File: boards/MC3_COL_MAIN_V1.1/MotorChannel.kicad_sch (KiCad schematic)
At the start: 8 parts, among them J7 MOTOR, U3 DRV8214RTER

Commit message: V1.1: encoder FFC VIN on filtered VSENS, motor pads off MotorChannel, yaw nets renamed
- Connectors: encoder FFC VIN now fed from VSENS (VM through FB61 + C63);
  ENC_leaf1-4 / RC_OUT labels re-placed; SIG pull-ups to +3V3 noted on sheet
- MotorChannel: J7-J9 MOTOR pad connectors (Conn_01x02) and their OUT1/OUT2
  hierarchical labels removed from the shared sheet
- MCU: ENC_leaf1-4 global labels re-placed; sheet notes carried over
- Root: H5 SLOT-PASSTHRU mounting hole removed
- PCB: yaw motor nets YAW_OUT* -> /yaw/OUT*; CANH/CANL pad assignment swapped;
  VSENS/VM net reassignments and follow-up routing (~106 segments, 12 vias,
  zone edits) to match the schematic

Co-Authored-By: Claude Fable 5 <noreply@anthropic.com>
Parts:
- removed J7: MOTOR, MC3_COL_MAIN:SolderPads_2x_2.2x1.4mm_P2.6mm, symbol Connector_Generic:Conn_01x02
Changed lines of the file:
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@@
-		)
-	)
-	(label "OUT1"
-		(at 144.78 95.25 180)
-		(effects
-			(font
-				(size 1.27 1.27)
-			)
-			(justify right bottom)
-		)
-	)
-	(label "OUT2"
-		(at 144.78 97.79 180)
-		(effects
-			(font
-				(size 1.27 1.27)
-			)
-			(justify right bottom)
 		)
 	)
@@
 				)
 			)
-		)
-	)
-	(hierarchical_label "OUT1"
-		(shape output)
-		(at 144.78 95.25 180)
-		(effects
-			(font
-				(size 1.27 1.27)
-			)
-			(justify right)
-		)
-	)
-	(hierarchical_label "OUT2"
-		(shape output)
-		(at 144.78 97.79 180)
-		(effects
-			(font
-				(size 1.27 1.27)
-			)
-			(justify right)
 		)
 	)
@@
 					(unit 1)
 				)
-			)
-		)
-	)
-	(symbol
-		(lib_id "Connector_Generic:Conn_01x02")
-		(at 149.86 95.25 0)
-		(unit 1)
-		(body_style 1)
-		(exclude_from_sim no)
-		(in_bom yes)
-		(on_board yes)
-		(in_pos_files yes)
-		(dnp no)
-		(property "Reference" "J7"
-			(at 149.86 92.71 0)
-			(show_name no)
-			(do_not_autoplace no)
-			(effects
-				(font
-					(size 1.27 1.27)
-				)
-			)
-		)
-		(property "Value" "MOTOR"
-			(at 149.86 100.33 0)
-			(show_name no)
-			(do_not_autoplace no)
-			(effects
-				(font
-					(size 1.27 1.27)
-				)
-			)
-		)
-		(property "Footprint" "MC3_COL_MAIN:SolderPads_2x_2.2x1.4mm_P2.6mm"
-			(at 149.86 95.25 0)
-			(hide yes)
-			(show_name no)
-			(do_not_autoplace no)
-			(effects
-				(font
-					(size 1.27 1.27)
-				)
-			)
-		)
-		(property "Datasheet" ""
-			(at 149.86 95.25 0)
-			(hide yes)
-			(show_name no)
-			(do_not_autoplace no)
-			(effects
-				(font
-					(size 1.27 1.27)
-				)
-			)
-		)
-		(property "Description" ""
-			(at 149.86 95.25 0)
-			(show_name no)
-			(do_not_autoplace no)
-			(effects
-				(font
-					(size 1.27 1.27)
-				)
-			)
-		)
-		(property "Note" "Bare solder pads 2.2x1.4 @2.6 mm, no part - vault Main-Board-01 Connectors, Motor Terminations"
-			(at 149.86 95.25 0)
-			(hide yes)
-			(show_name no)
-			(do_not_autoplace no)
-			(effects
-				(font
-					(size 1.27 1.27)
-				)
-			)
-		)
-		(pin "2"
-		)
-		(pin "1"
-		)
-		(instances
-			(project "MC3_COL_MAIN_V1.1"
-				(path "/7d5f4202-d55e-4c7b-a2df-dd599db38e48/5db6fbb9-0012-419b-b34a-9d86ac1f5217"
-					(reference "J8")
-					(unit 1)
-				)
-				(path "/7d5f4202-d55e-4c7b-a2df-dd599db38e48/8cfd3b4a-99dc-4b05-a7ad-f8199ec40931"
-					(reference "J11")
-					(unit 1)
-				)
-				(path "/7d5f4202-d55e-4c7b-a2df-dd599db38e48/9d20a086-3ce1-4783-a1c3-78685ff35655"
-					(reference "J10")
-					(unit 1)
-				)
-				(path "/7d5f4202-d55e-4c7b-a2df-dd599db38e48/a93ffbcb-09b2-46f4-87ff-b0a1b53638e4"
-					(reference "J7")
-					(unit 1)
-				)
-				(path "/7d5f4202-d55e-4c7b-a2df-dd599db38e48/f0c3363d-cc6b-4f74-be1d-ed0c2c093cdf"
-					(reference "J9")
-					(unit 1)
-				)
-			)
-			(project "MotorChannel"
-				(path "/d4aaa694-2c98-4a3a-bc8f-3a2af1030686"
-					(reference "J1")
-					(unit 1)
-				)

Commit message: V1.1: power routing pass — 24V chain + buck routed, stale-net/short fixes, VQFN corner pads fused, yaw OUT hier labels restored
- Board: VIN chain and buck cell routed (VIN_SW vias at Q1 source, SW between
  pads 8/9, boot via In2); ENC_leaf1 via at (83.9,97.075) renamed to ENC_leaf2;
  stray GND via under U1 strap deleted; VSENS via moved off the R32 rim arc;
  YAW_ENC_B gap closed at U9.1.
- MotorChannel.kicad_sch: OUT1/OUT2 hierarchical labels (passive) restored on
  the driver output wires; netlist verified YAW_OUT1/2 = U7 OUT + J13 5/6.
- VQFN-HR14_RJR_TEX: UL corner L-extensions were net-less F.Cu polygons over
  pads 1/5/9/11 (DRC overlap noise, parser-breaking width-0 strokes); fused
  into single rect pads covering the exact union; polys deleted. Board still
  carries the old embedded copy - Update Footprint on U12 pending.

Co-Authored-By: Claude Fable 5 <noreply@anthropic.com>
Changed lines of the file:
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@@
+		)
+	)
+	(hierarchical_label "OUT2"
+		(shape input)
+		(at 113.03 74.93 0)
+		(effects
+			(font
+				(size 1.27 1.27)
+			)
+			(justify left)
 		)
 	)
@@
 		)
 	)
+	(hierarchical_label "OUT1"
+		(shape input)
+		(at 113.03 72.39 0)
+		(effects
+			(font
+				(size 1.27 1.27)
+			)
+			(justify left)
+		)
+	)

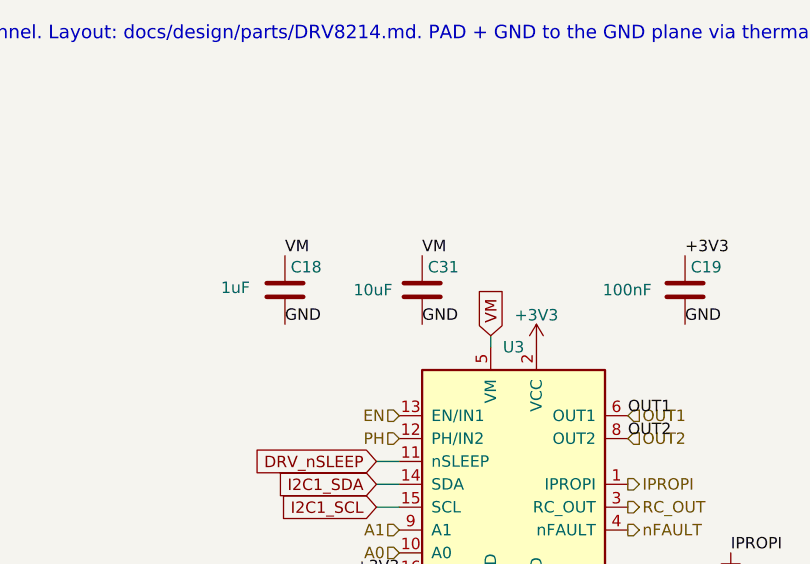
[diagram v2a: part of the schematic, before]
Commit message: Vault consolidation: Main-Board-02 rung folded back into Main-Board-01
Nothing was built at V1.0, so the 24 V revision never justified a rung bump.
Main-Board-01 now builds boards/MC3_COL_MAIN_V1.1 (24 V input); V1.0 stays in
the repo as the 5 V-only fallback revision. Repo side: CLAUDE.md rung mapping,
MIGRATION.md header and §14 pointer, LM61460 layout-note link. Vault side
(edited directly): Main-Board-01 Power rewritten as the 24 V chain, rung page
carries the V1.0→V1.1 delta/BOM/gates, Main-Board-02 folder deleted, 13 pages'
references rewritten.

Co-Authored-By: Claude Fable 5 <noreply@anthropic.com>
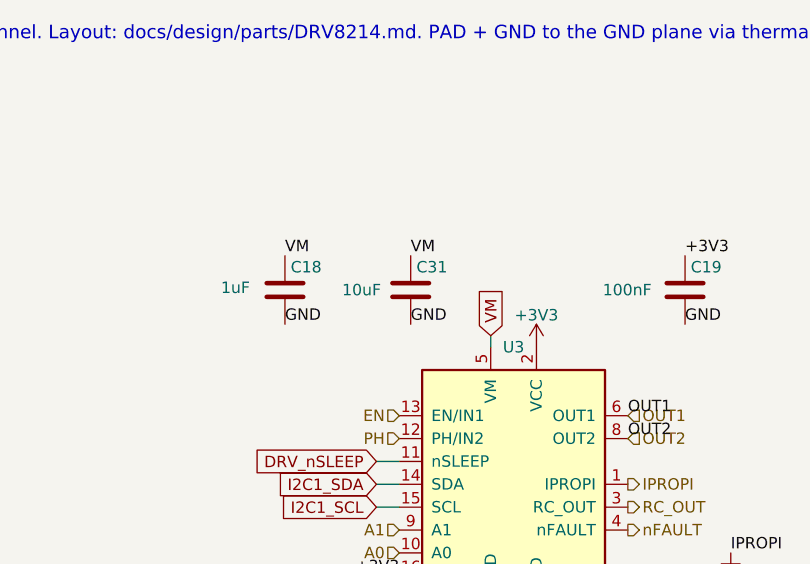
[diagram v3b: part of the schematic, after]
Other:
- moved on the sheet: C31
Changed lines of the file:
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@@
 	)
 	(label "VM"
-		(at 90.17 54.61 0)
+		(at 88.9 54.61 0)
 		(effects
 			(font
@@
 	)
 	(label "GND"
-		(at 90.17 62.23 0)
+		(at 88.9 62.23 0)
 		(effects
 			(font
@@
 	(symbol
 		(lib_id "Device:C")
-		(at 90.17 58.42 0)
+		(at 88.9 58.42 0)
 		(unit 1)
 		(body_style 1)
@@
 		(dnp no)
 		(property "Reference" "C31"
-			(at 90.805 55.88 0)
+			(at 89.535 55.88 0)
 			(show_name no)
 			(do_not_autoplace no)
@@
 		)
 		(property "Value" "10uF"
-			(at 82.55 58.42 0)
+			(at 81.28 58.42 0)
 			(show_name no)
 			(do_not_autoplace no)
@@
 		)
 		(property "Footprint" "MC3_COL_MAIN:C_0805_2012Metric"
-			(at 90.17 58.42 0)
+			(at 88.9 58.42 0)
 			(hide yes)
 			(show_name no)
@@
 		)
 		(property "Datasheet" ""
-			(at 90.17 58.42 0)
+			(at 88.9 58.42 0)
 			(hide yes)
 			(show_name no)
@@
 		)
 		(property "Description" ""
-			(at 90.17 58.42 0)
+			(at 88.9 58.42 0)
 			(show_name no)
 			(do_not_autoplace no)
@@
 		)
 		(property "LCSC" "C15850"
-			(at 90.17 58.42 0)
+			(at 88.9 58.42 0)
 			(hide yes)
 			(show_name no)
@@
 		)
 		(property "MPN" "CL21A106KAYNNNE"
-			(at 90.17 58.42 0)
+			(at 88.9 58.42 0)
 			(hide yes)
 			(show_name no)
@@
 		)
 		(property "Note" "Local VM bulk, one per channel. Added 2026-08-22: TI SLVSH04 asks for 0.1uF + bulk at VM; the board bulk (C3/C4) is in the power block, so the five bridges' di/dt was being supplied through the VM trunk inductance. 25V X5R keeps most of its value at the 5V rail. PROVISIONAL - value not set by a vault CALC"
-			(at 90.17 58.42 0)
-			(hide yes)
-			(show_name no)
+			(at 88.9 58.42 0)
+			(hide yes)
+			(show_name no)

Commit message: V1.1 schematics: per-instance Description fields on ~63 symbols
The component-docs Role source of record. Netlist unchanged, ERC 0.

Co-Authored-By: Claude Fable 5 <noreply@anthropic.com>
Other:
- note removed: "A1/A0 tri-level address straps are set per instance on the root sheet (GND / +3V3)."
- note removed: "Motor channel - one per leaf, instantiated x4. Implements: COL-COTS-0028 (DRV8214, integrated current sense + ripple counting) - vault Main-Board-01 Motor Channel. Layout: docs/design/parts/DRV8214.md. PAD + GND to the GND plane via thermal vias. VREF = +3V3 (TI typical app). PROVISIONAL: R_IPROPI, pull-ups."
- note removed: "Review 2026-08-22: R_IPROPI 6.8k -> hardware current trip 1.99 A (was 8.45k -> 1.60 A)."
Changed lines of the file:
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@@
 	(generator_version "10.0")
 	(paper "A4")
-	(text "Motor channel - one per leaf, instantiated x4. Implements: COL-COTS-0028 (DRV8214, integrated current sense + ripple counting) - vault Main-Board-01 Motor Channel. Layout: docs/design/parts/DRV8214.md. PAD + GND to the GND plane via thermal vias. VREF = +3V3 (TI typical app). PROVISIONAL: R_IPROPI, pull-ups."
-		(exclude_from_sim no)
-		(at 40 30 0)
-		(effects
-			(font
-				(size 1.5 1.5)
-			)
-		)
-	)
-	(text "Review 2026-08-22: R_IPROPI 6.8k -> hardware current trip 1.99 A (was 8.45k -> 1.60 A)."
-		(exclude_from_sim no)
-		(at 94.742 120.316 0)
-		(effects
-			(font
-				(size 1.5 1.5)
-			)
-		)
-	)
-	(text "A1/A0 tri-level address straps are set per instance on the root sheet (GND / +3V3)."
-		(exclude_from_sim no)
-		(at 94.742 115.316 0)
-		(effects
-			(font
-				(size 1.5 1.5)
-			)
-		)
-	)
 	(wire
 		(pts
@@
 		)
 	)
-	(label "OUT2"
-		(at 113.03 74.93 0)
-		(effects
-			(font
-				(size 1.27 1.27)
-			)
-			(justify left bottom)
-		)
-	)
 	(label "+3V3"
 		(at 87.63 90.17 180)
@@
 	(label "VM"
 		(at 88.9 54.61 0)
-		(effects
-			(font
-				(size 1.27 1.27)
-			)
-			(justify left bottom)
-		)
-	)
-	(label "OUT1"
-		(at 113.03 72.39 0)
 		(effects
 			(font
@@
 			)
 		)
-		(property "Description" ""
+		(property "Description" "IPROPI sense resistor 6.8 k — 1.66 V/A, hardware current trip I_TRIP ≈ 1.99 A (shared across the five channels)."
 			(at 124.46 91.44 0)
 			(show_name no)
@@
 			)
 		)
-		(property "Description" ""
+		(property "Description" "DRV8214 H-bridge [[COL-COTS-0028]] — one per axis (shared sheet: U3–U7); integrated current sense, ripple counting, I²C config. Layout: docs/design/parts/DRV8214.md."
 			(at 100.33 80.01 0)
 			(show_name no)
